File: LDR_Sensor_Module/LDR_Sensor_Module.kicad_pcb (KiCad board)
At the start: 2 copper layers, 36.5 x 19.5 mm, 13 parts, among them J1 Conn_01x04, U1 LM393

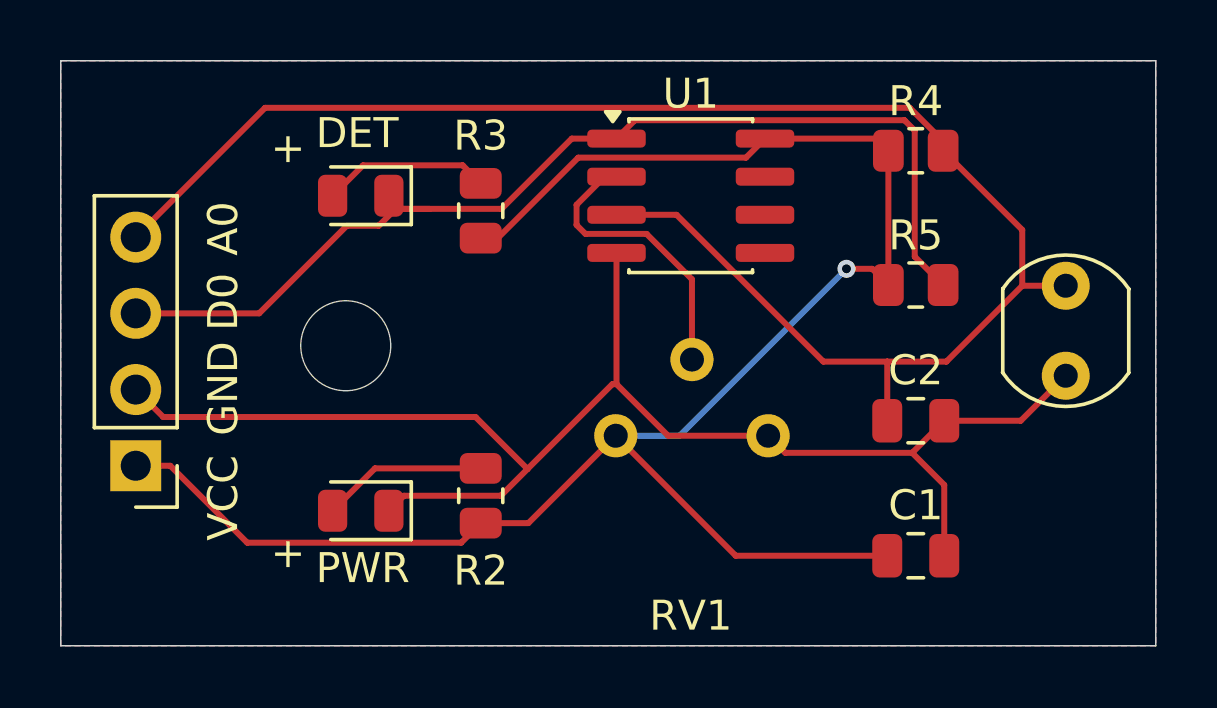
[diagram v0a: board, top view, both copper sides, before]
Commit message: Modified LDR Sensor Module
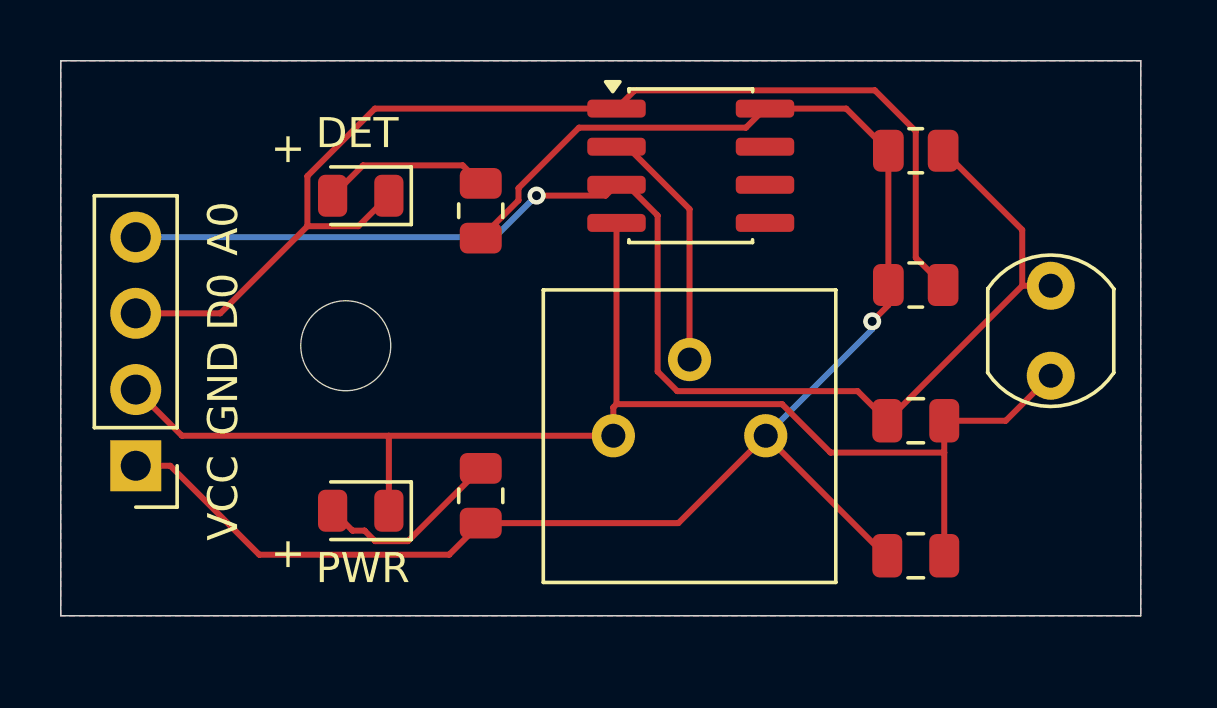
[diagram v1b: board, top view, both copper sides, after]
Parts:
- RV1: moved to F.Cu
- moved RV1 5.00 mm to (105.0, 100.0)
- moved U1 1.00 mm to (102.5, 91.0)
- moved R1 0.50 mm to (114.5, 95.0)
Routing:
- net /A0: track 55.1 -> 45.0 mm, vias 0 -> 1
- net VCC: track 60.5 -> 57.0 mm
- net /D0: track 35.8 -> 39.3 mm
- net GND: track 48.7 -> 46.5 mm
- net Net-(U1A--): track 9.66 -> 8.31 mm
- net Net-(D1-A): track 5.52 -> 6.36 mm
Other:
- board size 36.5 x 19.5 mm -> 36 x 18.5 mm
